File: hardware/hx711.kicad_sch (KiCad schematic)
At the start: 20 parts, among them J2 M05PTH, Q1 MMBT4403, U5 HX711

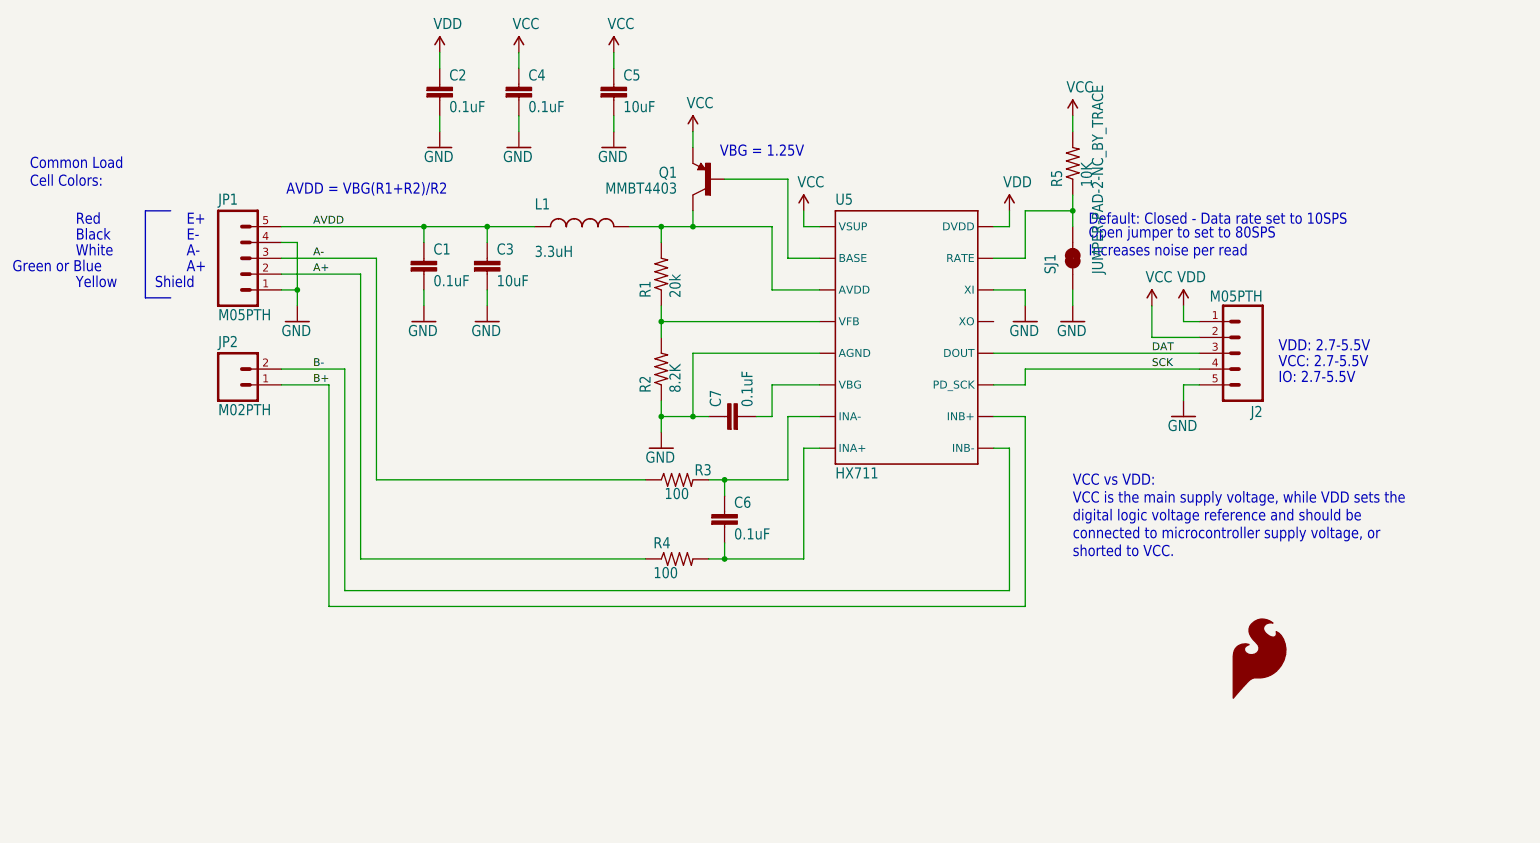
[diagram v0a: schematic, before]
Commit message: Integrate HX711 sub-schematic
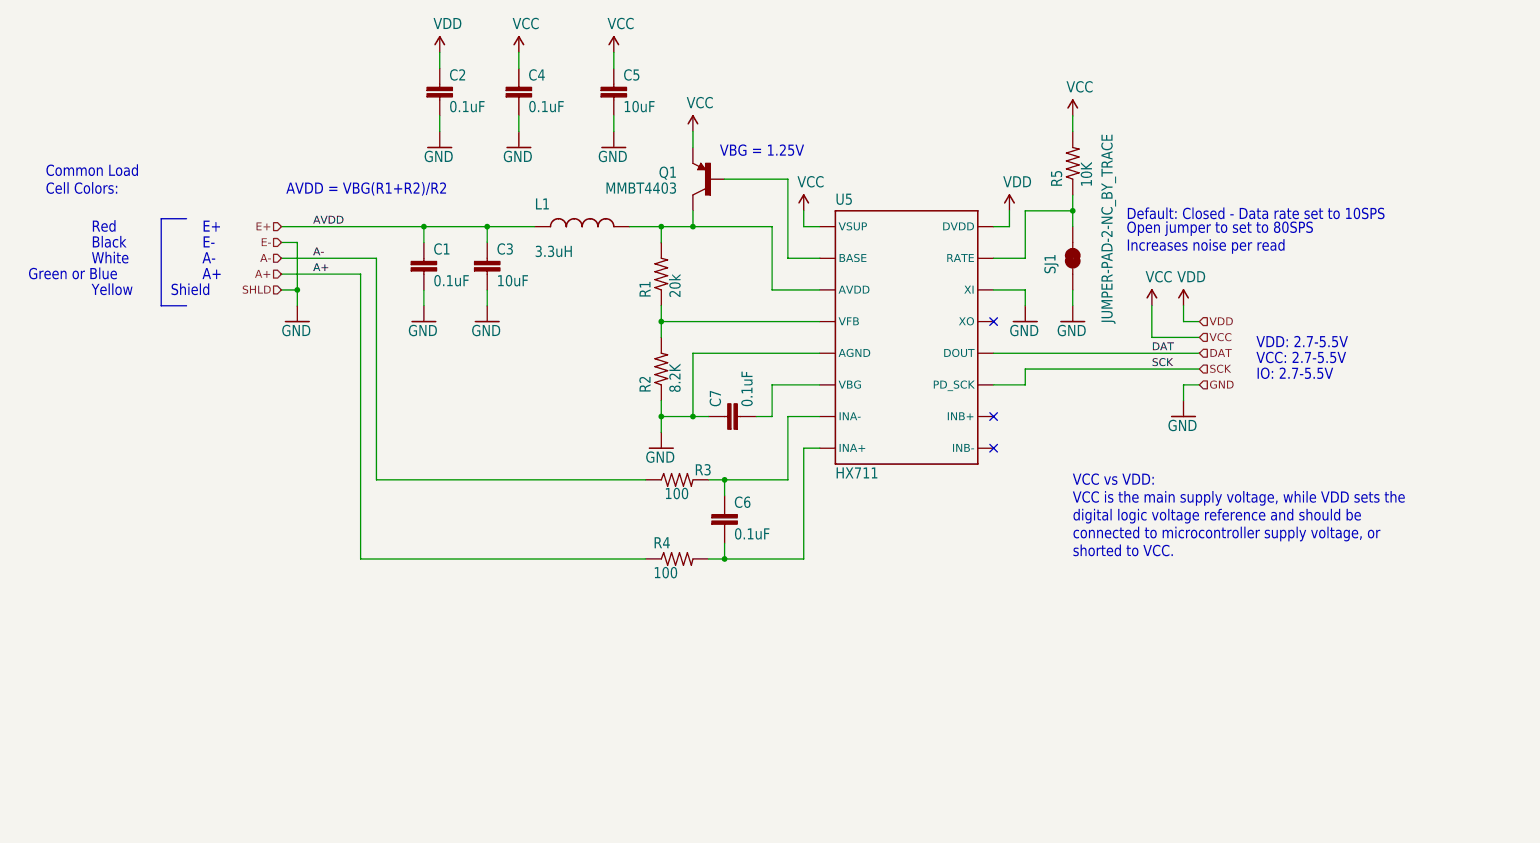
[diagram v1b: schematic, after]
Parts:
- removed J2, JP1: M05PTH, Sparkfun-HX711:1X05, symbol Sparkfun-HX711-eagle-import:M05PTH
- removed JP2: M02PTH, Sparkfun-HX711:1X02, symbol Sparkfun-HX711-eagle-import:M02PTH
- removed LOGO1: SFE_LOGO_FLAME.1_INCH, Sparkfun-HX711:SFE_LOGO_FLAME_.1, symbol Sparkfun-HX711-eagle-import:SFE_LOGO_FLAME.1_INCH
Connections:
- net AVDD renamed E+
- net B+: no longer names the net of U5.10 (INB+)
- net B-: no longer names the net of U5.9 (INB-)
- no-connect marks 0 -> 3

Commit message: Finish HX711 integration
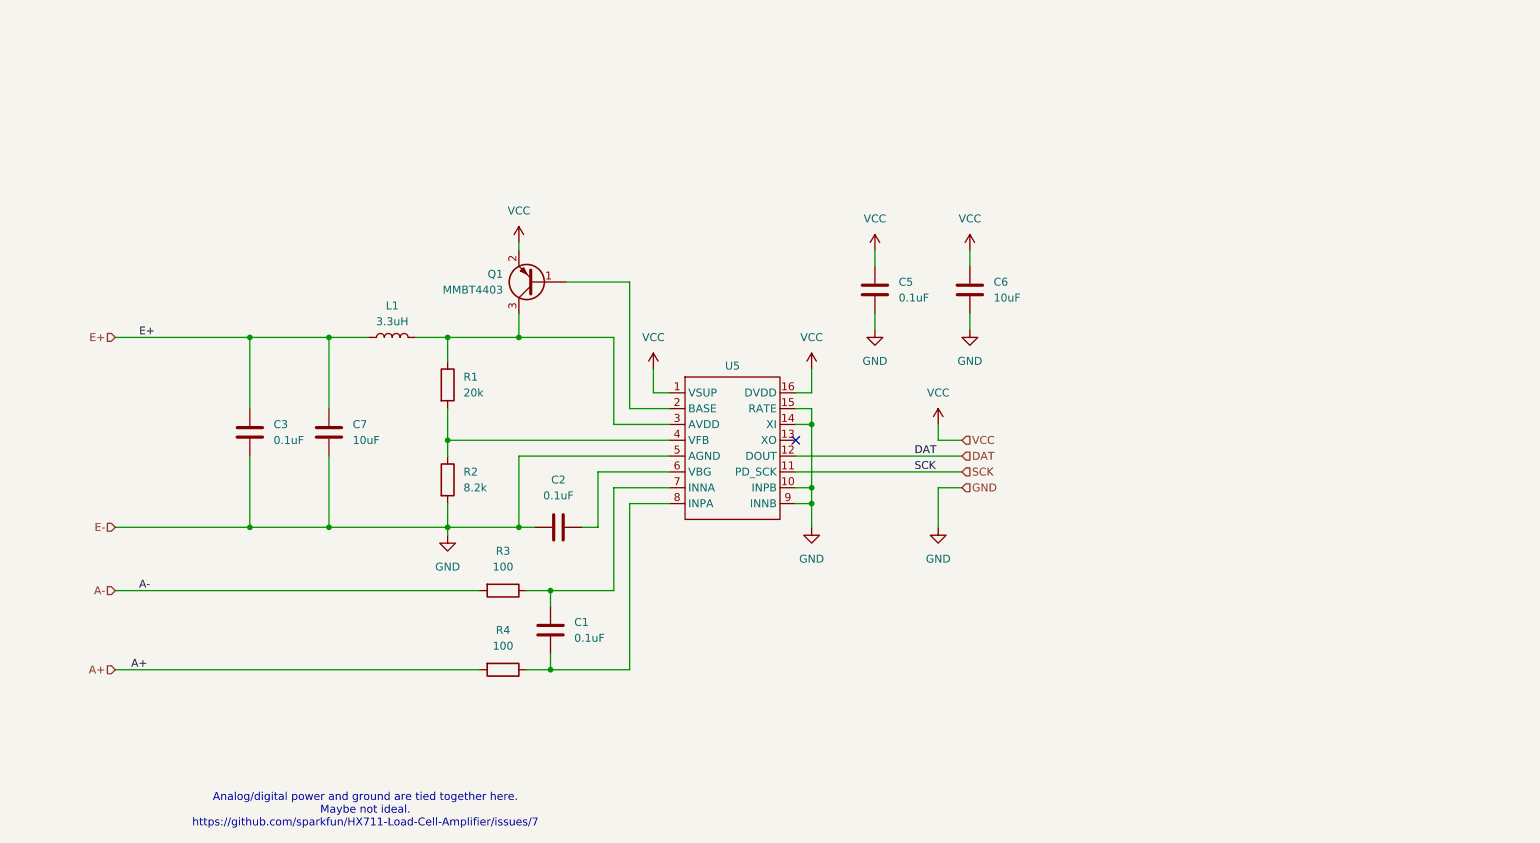
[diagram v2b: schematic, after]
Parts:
- removed C1, C2, C4, C6, C7: 0.1uF, Sparkfun-HX711:0603-CAP, symbol Sparkfun-HX711-eagle-import:0.1UF-25V-5%(0603)
- removed C3, C5: 10uF, Sparkfun-HX711:1210, symbol Sparkfun-HX711-eagle-import:10UF50V20%(1210)
- removed L1: 3.3uH, Sparkfun-HX711:0805, symbol Sparkfun-HX711-eagle-import:INDUCTOR0805-IND
- removed Q1: MMBT4403, Sparkfun-HX711:SOT23-3, symbol Sparkfun-HX711-eagle-import:TRANSISTOR_PNPMMBT4403
- removed R1: 20k, Sparkfun-HX711:0603-RES, symbol Sparkfun-HX711-eagle-import:20KOHM1/10W1%(0603)
- removed R2: 8.2K, Sparkfun-HX711:0603-RES, symbol Sparkfun-HX711-eagle-import:8.2KOHM-1/10W-5%(0603)
- removed R3, R4: 100, Sparkfun-HX711:0603-RES, symbol Sparkfun-HX711-eagle-import:100OHM-1/10W-1%(0603)
- removed R5: 10K, Sparkfun-HX711:0603-RES, symbol Sparkfun-HX711-eagle-import:10KOHM-1/10W-1%(0603)0603
- removed SJ1: JUMPER-PAD-2-NC_BY_TRACE, Sparkfun-HX711:PAD-JUMPER-2-NC_BY_TRACE_YES_SILK, symbol Sparkfun-HX711-eagle-import:JUMPER-PAD-2-NC_BY_TRACE
- removed U5: HX711, Sparkfun-HX711:SO16, symbol Sparkfun-HX711-eagle-import:HX711HX711
- added C1, C2, C3, C5: 0.1uF, Capacitor_SMD:C_0603_1608Metric, symbol Device:C
- added C6, C7: 10uF, Capacitor_SMD:C_1210_3225Metric, symbol Device:C
- added L1: 3.3uH, Inductor_SMD:L_0805_2012Metric, symbol Device:L
- added Q1: MMBT4403, Package_TO_SOT_SMD:TSOT-23, symbol Device:Q_PNP_BEC
- added R1: 20k, Resistor_SMD:R_0603_1608Metric, symbol Device:R
- added R2: 8.2k, Resistor_SMD:R_0603_1608Metric, symbol Device:R
- added R3, R4: 100, Resistor_SMD:R_0603_1608Metric, symbol Device:R
- added U5: ~, Package_SO:SOP-16_3.9x9.9mm_P1.27mm, symbol CoffeeLib:HX711
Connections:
- net A+: now also R4.2
- net A-: now also R3.2
- net DAT: now also U5.12 (DOUT)
- net E+: now also C3.1, C7.1, L1.1
- net GND: now also C2.1, C3.2, C5.2, C6.2, C7.2, R2.2, U5.10 (INPB), U5.14 (XI), U5.15 (RATE), U5.5 (AGND), U5.9 (INNB)
- net SCK: now also U5.11 (PD_SCK)
- net VCC: now also C5.1, C6.1, Q1.2 (E), U5.1 (VSUP), U5.16 (DVDD)
- new net: C1.2, R4.1, U5.8 (INPA)
- new net: C1.1, R3.1, U5.7 (INNA)
- new net: Q1.1 (B), U5.2 (BASE)
- new net: L1.2, Q1.3 (C), R1.1, U5.3 (AVDD)
- new net: R1.2, R2.1, U5.4 (VFB)
- new net: C2.2, U5.6 (VBG)
- no-connect marks 3 -> 1
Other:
- note added: "Analog/digital power and ground are tied together here. Maybe not ideal. https://github.com/sparkfun/HX711-Load-Cell-Amplifier/issues/7"
- note removed: "A+"
- note removed: "A-"
- note removed: "AVDD = VBG(R1+R2)/R2"
- note removed: "Black"
- note removed: "Common Load Cell Colors:"
- note removed: "Default: Closed - Data rate set to 10SPS"
- note removed: "E+"
- note removed: "E-"
- note removed: "Green or Blue"
- note removed: "IO: 2.7-5.5V"
- note removed: "Open jumper to set to 80SPS Increases noise per read"
- note removed: "Red"
- note removed: "Shield"
- note removed: "VBG = 1.25V"
- note removed: "VCC vs VDD: VCC is the main supply voltage, while VDD sets the digital logic voltage reference and should be connected to microcontroller supply voltage, or shorted to VCC."
- note removed: "VCC: 2.7-5.5V"
- note removed: "VDD: 2.7-5.5V"
- note removed: "White"
- note removed: "Yellow"

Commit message: Create analog ground plane for HX711
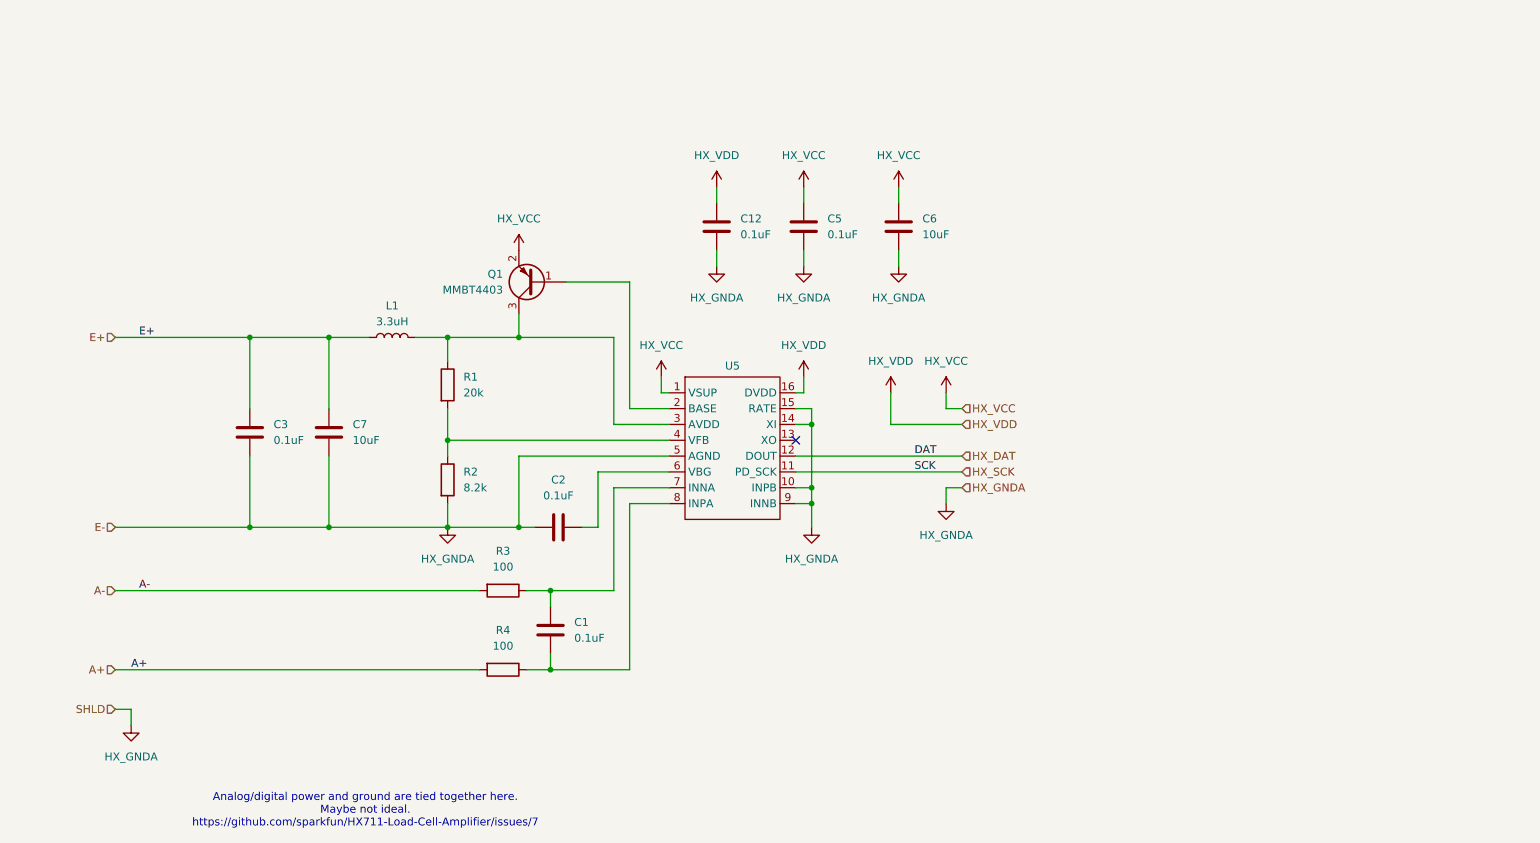
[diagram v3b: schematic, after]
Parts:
- added C12: 0.1uF, Capacitor_SMD:C_0603_1608Metric, symbol Device:C
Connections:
- net DAT renamed HX_DAT
- net GND renamed HX_GNDA
- net HX_GNDA: now also C12.2
- net SCK renamed HX_SCK
- net VCC renamed HX_VCC
- net HX_VCC: no longer U5.16 (DVDD)
- new net HX_VDD: C12.1, U5.16 (DVDD)
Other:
- moved on the sheet: C5, C6

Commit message: Infinite schematic/PCB changes
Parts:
- removed C6: 10uF, Capacitor_SMD:C_1210_3225Metric, symbol Device:C
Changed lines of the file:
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@@
-	(wire
-		(pts
-			(xy 186.69 66.04) (xy 186.69 63.5)
-		)
-		(stroke
-			(width 0.1524)
-			(type solid)
-		)
-	)
 	(wire
 		(pts
@@
 		(pts
 			(xy 114.3 106.68) (xy 114.3 104.14)
-		)
-		(stroke
-			(width 0.1524)
-			(type solid)
-		)
-	)
-	(wire
-		(pts
-			(xy 186.69 73.66) (xy 186.69 76.2)
 		)
 		(stroke
@@
 	)
 	(symbol
-		(lib_id "power:VCC")
-		(at 186.69 63.5 0)
-		(unit 1)
-		(exclude_from_sim no)
-		(in_bom yes)
-		(on_board yes)
-		(dnp no)
-		(fields_autoplaced yes)
-		(property "Reference" "#PWR018"
-			(at 186.69 67.31 0)
-			(effects
-				(font
-					(size 1.27 1.27)
-				)
-				(hide yes)
-			)
-		)
-		(property "Value" "HX_VCC"
-			(at 186.69 58.42 0)
-			(effects
-				(font
-					(size 1.27 1.27)
-				)
-			)
-		)
-		(property "Footprint" ""
-			(at 186.69 63.5 0)
-			(effects
-				(font
-					(size 1.27 1.27)
-				)
-				(hide yes)
-			)
-		)
-		(property "Datasheet" ""
-			(at 186.69 63.5 0)
-			(effects
-				(font
-					(size 1.27 1.27)
-				)
-				(hide yes)
-			)
-		)
-		(property "Description" "Power symbol creates a global label with name \"VCC\""
-			(at 186.69 63.5 0)
-			(effects
-				(font
-					(size 1.27 1.27)
-				)
-				(hide yes)
-			)
-		)
-		(pin "1"
-		)
-		(instances
-			(project "coffee-scales"
-				(path "/2c28a4aa-0841-4fd8-a9c6-3f977db869be/1d428739-d68e-4adc-8d4c-778c2f9df208"
-					(reference "#PWR018")
-					(unit 1)
-				)
-			)
-		)
-	)
-	(symbol
 		(lib_id "Device:C")
 		(at 130.81 134.62 0)
@@
 	(symbol
 		(lib_id "power:GNDA")
-		(at 186.69 76.2 0)
-		(unit 1)
-		(exclude_from_sim no)
-		(in_bom yes)
-		(on_board yes)
-		(dnp no)
-		(fields_autoplaced yes)
-		(property "Reference" "#PWR022"
-			(at 186.69 82.55 0)
-			(effects
-				(font
-					(size 1.27 1.27)
-				)
-				(hide yes)
-			)
-		)
-		(property "Value" "HX_GNDA"
-			(at 186.69 81.28 0)
-			(effects
-				(font
-					(size 1.27 1.27)
-				)
-			)
-		)
-		(property "Footprint" ""
-			(at 186.69 76.2 0)
-			(effects
-				(font
-					(size 1.27 1.27)
-				)
-				(hide yes)
-			)
-		)
-		(property "Datasheet" ""
-			(at 186.69 76.2 0)
-			(effects
-				(font
-					(size 1.27 1.27)
-				)
-				(hide yes)
-			)
-		)
-		(property "Description" "Power symbol creates a global label with name \"GNDA\" , analog ground"
-			(at 186.69 76.2 0)
-			(effects
-				(font
-					(size 1.27 1.27)
-				)
-				(hide yes)
-			)
-		)
-		(pin "1"
-		)
-		(instances
-			(project "coffee-scales"
-				(path "/2c28a4aa-0841-4fd8-a9c6-3f977db869be/1d428739-d68e-4adc-8d4c-778c2f9df208"
-					(reference "#PWR022")
-					(unit 1)
-				)
-			)
-		)
-	)
-	(symbol
-		(lib_id "power:GNDA")
 		(at 171.45 76.2 0)
 		(unit 1)
@@
 					(unit 1)
 				)
-			)
-		)
-	)
-	(symbol
-		(lib_id "Device:C")
-		(at 186.69 69.85 0)
-		(unit 1)
-		(exclude_from_sim no)
-		(in_bom yes)
-		(on_board yes)
-		(dnp no)
-		(fields_autoplaced yes)
-		(property "Reference" "C6"
-			(at 190.5 68.5799 0)
-			(effects
-				(font
-					(size 1.27 1.27)
-				)
-				(justify left)
-			)
-		)
-		(property "Value" "10uF"
-			(at 190.5 71.1199 0)
-			(effects
-				(font
-					(size 1.27 1.27)
-				)
-				(justify left)
-			)
-		)
-		(property "Footprint" "Capacitor_SMD:C_1210_3225Metric"
-			(at 187.6552 73.66 0)
-			(effects
-				(font
-					(size 1.27 1.27)
-				)
-				(hide yes)
-			)
-		)
-		(property "Datasheet" "~"
-			(at 186.69 69.85 0)
-			(effects
-				(font
-					(size 1.27 1.27)
-				)
-				(hide yes)
-			)
-		)
-		(property "Description" "Unpolarized capacitor"
-			(at 186.69 69.85 0)
-			(effects
-				(font
-					(size 1.27 1.27)
-				)
-				(hide yes)
-			)
-		)
-		(pin "1"
-		)
-		(pin "2"
-		)
-		(instances
-			(project "coffee-scales"
-				(path "/2c28a4aa-0841-4fd8-a9c6-3f977db869be/1d428739-d68e-4adc-8d4c-778c2f9df208"
-					(reference "C6")
-					(unit 1)
-				)

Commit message: Keep hacking
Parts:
- renumbered C7 to C10, C12 to C5, C2 to C6, C1 to C7, C5 to C8, C3 to C9, R3 to R2, R4 to R3, R1 to R4, R2 to R5, U5 to U2
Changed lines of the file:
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@@
 		(dnp no)
 		(fields_autoplaced yes)
-		(property "Reference" "C3"
+		(property "Reference" "C9"
 			(at 86.36 101.5999 0)
 			(effects
@@
 			(project ""
 				(path "/2c28a4aa-0841-4fd8-a9c6-3f977db869be/1d428739-d68e-4adc-8d4c-778c2f9df208"
-					(reference "C3")
+					(reference "C9")
 					(unit 1)
 				)
@@
 		(dnp no)
 		(fields_autoplaced yes)
-		(property "Reference" "R4"
+		(property "Reference" "R3"
 			(at 123.19 134.62 90)
 			(effects
@@
 			(project "coffee-scales"
 				(path "/2c28a4aa-0841-4fd8-a9c6-3f977db869be/1d428739-d68e-4adc-8d4c-778c2f9df208"
-					(reference "R4")
+					(reference "R3")
 					(unit 1)
 				)
@@
 		(dnp no)
 		(fields_autoplaced yes)
-		(property "Reference" "R3"
+		(property "Reference" "R2"
 			(at 123.19 121.92 90)
 			(effects
@@
 			(project "coffee-scales"
 				(path "/2c28a4aa-0841-4fd8-a9c6-3f977db869be/1d428739-d68e-4adc-8d4c-778c2f9df208"
-					(reference "R3")
+					(reference "R2")
 					(unit 1)
 				)
@@
 		(dnp no)
 		(fields_autoplaced yes)
-		(property "Reference" "C7"
+		(property "Reference" "C10"
 			(at 99.06 101.5999 0)
 			(effects
@@
 			(project "coffee-scales"
 				(path "/2c28a4aa-0841-4fd8-a9c6-3f977db869be/1d428739-d68e-4adc-8d4c-778c2f9df208"
-					(reference "C7")
+					(reference "C10")
 					(unit 1)
 				)
@@
 		(dnp no)
 		(fields_autoplaced yes)
-		(property "Reference" "C5"
+		(property "Reference" "C8"
 			(at 175.26 68.5799 0)
 			(effects
@@
 			(project "coffee-scales"
 				(path "/2c28a4aa-0841-4fd8-a9c6-3f977db869be/1d428739-d68e-4adc-8d4c-778c2f9df208"
-					(reference "C5")
+					(reference "C8")
 					(unit 1)
 				)
@@
 		(on_board yes)
 		(dnp no)
-		(property "Reference" "U5"
+		(property "Reference" "U2"
 			(at 160.02 92.202 0)
 			(effects
@@
 			(project ""
 				(path "/2c28a4aa-0841-4fd8-a9c6-3f977db869be/1d428739-d68e-4adc-8d4c-778c2f9df208"
-					(reference "U5")
+					(reference "U2")
 					(unit 1)
 				)
@@
 		(dnp no)
 		(fields_autoplaced yes)
-		(property "Reference" "C12"
+		(property "Reference" "C5"
 			(at 161.29 68.5799 0)
 			(effects
@@
 			(project "coffee-scales"
 				(path "/2c28a4aa-0841-4fd8-a9c6-3f977db869be/1d428739-d68e-4adc-8d4c-778c2f9df208"
-					(reference "C12")
+					(reference "C5")
 					(unit 1)
 				)
@@
 		(dnp no)
 		(fields_autoplaced yes)
-		(property "Reference" "R1"
+		(property "Reference" "R4"
 			(at 116.84 93.9799 0)
 			(effects
@@
 			(project ""
 				(path "/2c28a4aa-0841-4fd8-a9c6-3f977db869be/1d428739-d68e-4adc-8d4c-778c2f9df208"
-					(reference "R1")
+					(reference "R4")
 					(unit 1)
 				)
@@
 		(dnp no)
 		(fields_autoplaced yes)
-		(property "Reference" "C2"
+		(property "Reference" "C6"
 			(at 132.08 110.49 90)
 			(effects
@@
 			(project "coffee-scales"
 				(path "/2c28a4aa-0841-4fd8-a9c6-3f977db869be/1d428739-d68e-4adc-8d4c-778c2f9df208"
-					(reference "C2")
+					(reference "C6")
 					(unit 1)
 				)
@@
 		(dnp no)
 		(fields_autoplaced yes)
-		(property "Reference" "C1"
+		(property "Reference" "C7"
 			(at 134.62 133.3499 0)
 			(effects
@@
 			(project "coffee-scales"
 				(path "/2c28a4aa-0841-4fd8-a9c6-3f977db869be/1d428739-d68e-4adc-8d4c-778c2f9df208"
-					(reference "C1")
+					(reference "C7")
 					(unit 1)
 				)
@@
 		(dnp no)
 		(fields_autoplaced yes)
-		(property "Reference" "R2"
+		(property "Reference" "R5"
 			(at 116.84 109.2199 0)
 			(effects
@@
 			(project "coffee-scales"
 				(path "/2c28a4aa-0841-4fd8-a9c6-3f977db869be/1d428739-d68e-4adc-8d4c-778c2f9df208"
-					(reference "R2")
-					(unit 1)
-				)
+					(reference "R5")
+					(unit 1)
+				)
